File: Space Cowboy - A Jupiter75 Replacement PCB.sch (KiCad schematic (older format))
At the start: 200 parts, among them SW1 SW_PUSH, U1 ATmega32U4-AU, Y1 16MHz

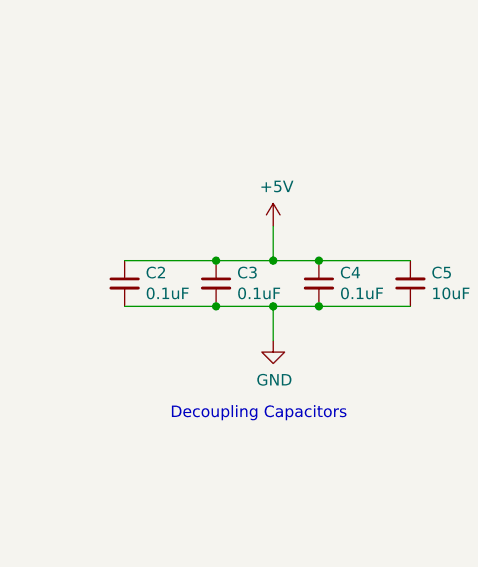
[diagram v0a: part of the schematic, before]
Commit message: Update Space Cowboy - A Jupiter75 Replacement PCB.sch
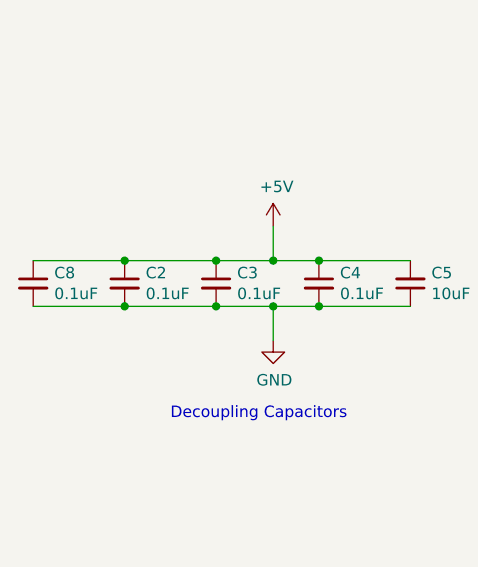
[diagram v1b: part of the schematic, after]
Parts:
- added C8: 0.1uF, Capacitors_SMD:C_0603, symbol Device:C_Small
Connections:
- net +5V: now also C8.1
- net GND: now also C8.2
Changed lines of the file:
@@
 Text GLabel 4750 8300 2    50   Input ~ 0
 ROW1
+$Comp
+L Device:C_Small C8
+U 1 1 5FEDD851
+P 800 9650
+F 0 "C8" H 892 9696 50  0000 L CNN
+F 1 "0.1uF" H 892 9605 50  0000 L CNN
+F 2 "Capacitors_SMD:C_0603" H 800 9650 50  0001 C CNN
+F 3 "~" H 800 9650 50  0001 C CNN
+	1    800  9650
+	1    0    0    -1
+$EndComp
+Wire Wire Line
+	800  9550 1200 9550
+Connection ~ 1200 9550
+Wire Wire Line
+	800  9750 1200 9750
+Connection ~ 1200 9750
 $EndSCHEMATC
